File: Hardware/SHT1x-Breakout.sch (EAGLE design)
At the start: 9 parts, among them U1 SHT1XSMD

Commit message: Initial Revision Commit
Testing to make sure changes only happen to V_1.4 branch. Initial
layout of new revision.
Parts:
- removed R2: 10K, SparkFun:RESISTOR0603-RES
- removed U$1: LOGO-SFENEW, SparkFun:LOGO-SFENEW
- removed U$2, U$3: FIDUCIAL1X2, SparkFun:FIDUCIAL1X2
- added FID1, FID2: FIDUCIAL1X2, SparkFun-Aesthetics:FIDUCIAL1X2
- added FRAME1: (no value), SparkFun-Aesthetics:FRAME-LETTER
- added LOGO1: OSHW-LOGOS, SparkFun-Aesthetics:OSHW-LOGOS
- added LOGO4: SFE_LOGO_FLAME.1_INCH, SparkFun-Aesthetics:SFE_LOGO_FLAME.1_INCH
- added SJ1: JUMPER-PAD-2-NC_BY_TRACE, SparkFun-Passives:JUMPER-PAD-2-NC_BY_TRACE
- added STANDOFF1, STANDOFF2: STAND-OFF, SparkFun-Electromechanical:STAND-OFF
- C1: device SparkFun:CAP0603-CAP -> SparkFun-Capacitors:0.1UF-25V(+80/-20%)(0603)
- R1: device SparkFun:RESISTOR0603-RES -> SparkFun-Resistors:10KOHM-1/10W-1%(0603)0603
- U1: device SparkFun:SHT1XSMD -> SparkFun-Sensors:SHT1XSMD
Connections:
- removed net VDD: C1.2, JP1.1, R1.2, U1.VDD
- new net N$1: R1.1, SJ1.1
- new net VCC: C1.1, JP1.3, R1.2, U1.VDD
- net DATA: now also SJ1.2; no longer R1.1
- net GND: now also C1.2; no longer C1.1, R2.2
- net SCK: now also JP1.1; no longer JP1.3, R2.1
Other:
- note added: "Connector"
- note added: "However, it can live on an I2C bus with other I2C devices without interfering."
- note added: "Pull-up Resistor"
- note added: "Sht_15 Sensor"
- note added: "The SHT_15 communicates using a 2-wire Serial Protocol, NOT I2C."
- note removed: "01"
- note removed: "Not Populated"
- note removed: "SHT1x Breakout Board"
- moved on the sheet: C1, JP1, R1, U1

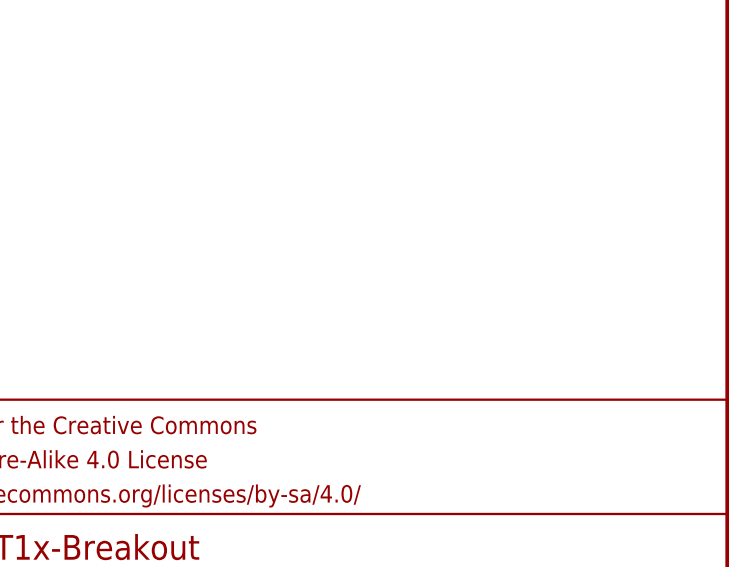
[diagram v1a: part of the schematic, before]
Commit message: Initial Layout finished
Initial Layout finished - ready for monday review
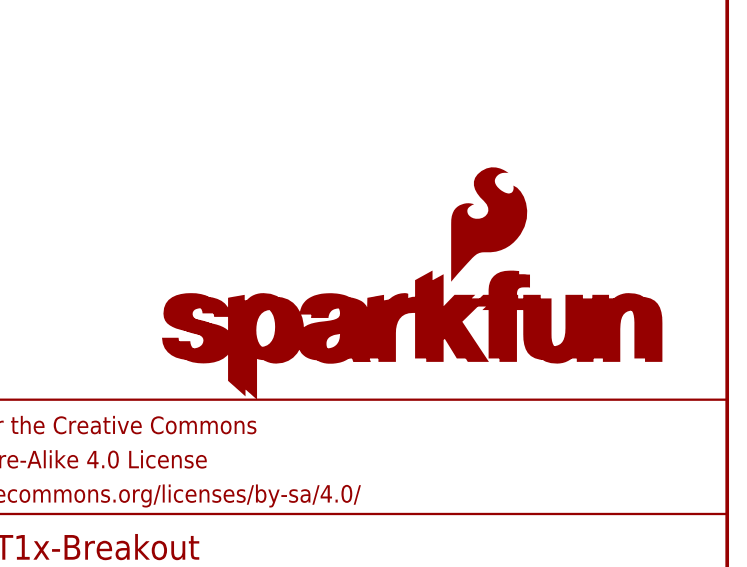
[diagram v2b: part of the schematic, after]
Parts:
- added LOGO2: SFE_LOGO_NAME.1_INCH, SparkFun-Aesthetics:SFE_LOGO_NAME.1_INCH
- added LOGO5: SFE_LOGO_NAME_FLAME.1_INCH, SparkFun-Aesthetics:SFE_LOGO_NAME_FLAME.1_INCH
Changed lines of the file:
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@@
 <part name="LOGO4" library="SparkFun-Aesthetics" deviceset="SFE_LOGO_FLAME" device=".1_INCH"/>
 <part name="P+2" library="SparkFun" deviceset="VCC" device=""/>
+<part name="LOGO2" library="SparkFun-Aesthetics" deviceset="SFE_LOGO_NAME" device=".1_INCH"/>
+<part name="LOGO5" library="SparkFun-Aesthetics" deviceset="SFE_LOGO_NAME_FLAME" device=".1_INCH"/>
 </parts>
 <sheets>
@@
 <instance part="LOGO4" gate="G$1" x="114.3" y="2.54"/>
 <instance part="P+2" gate="1" x="142.24" y="154.94"/>
+<instance part="LOGO2" gate="G$1" x="185.42" y="35.56"/>
+<instance part="LOGO5" gate="G$1" x="185.42" y="35.56"/>
 </instances>
 <busses>

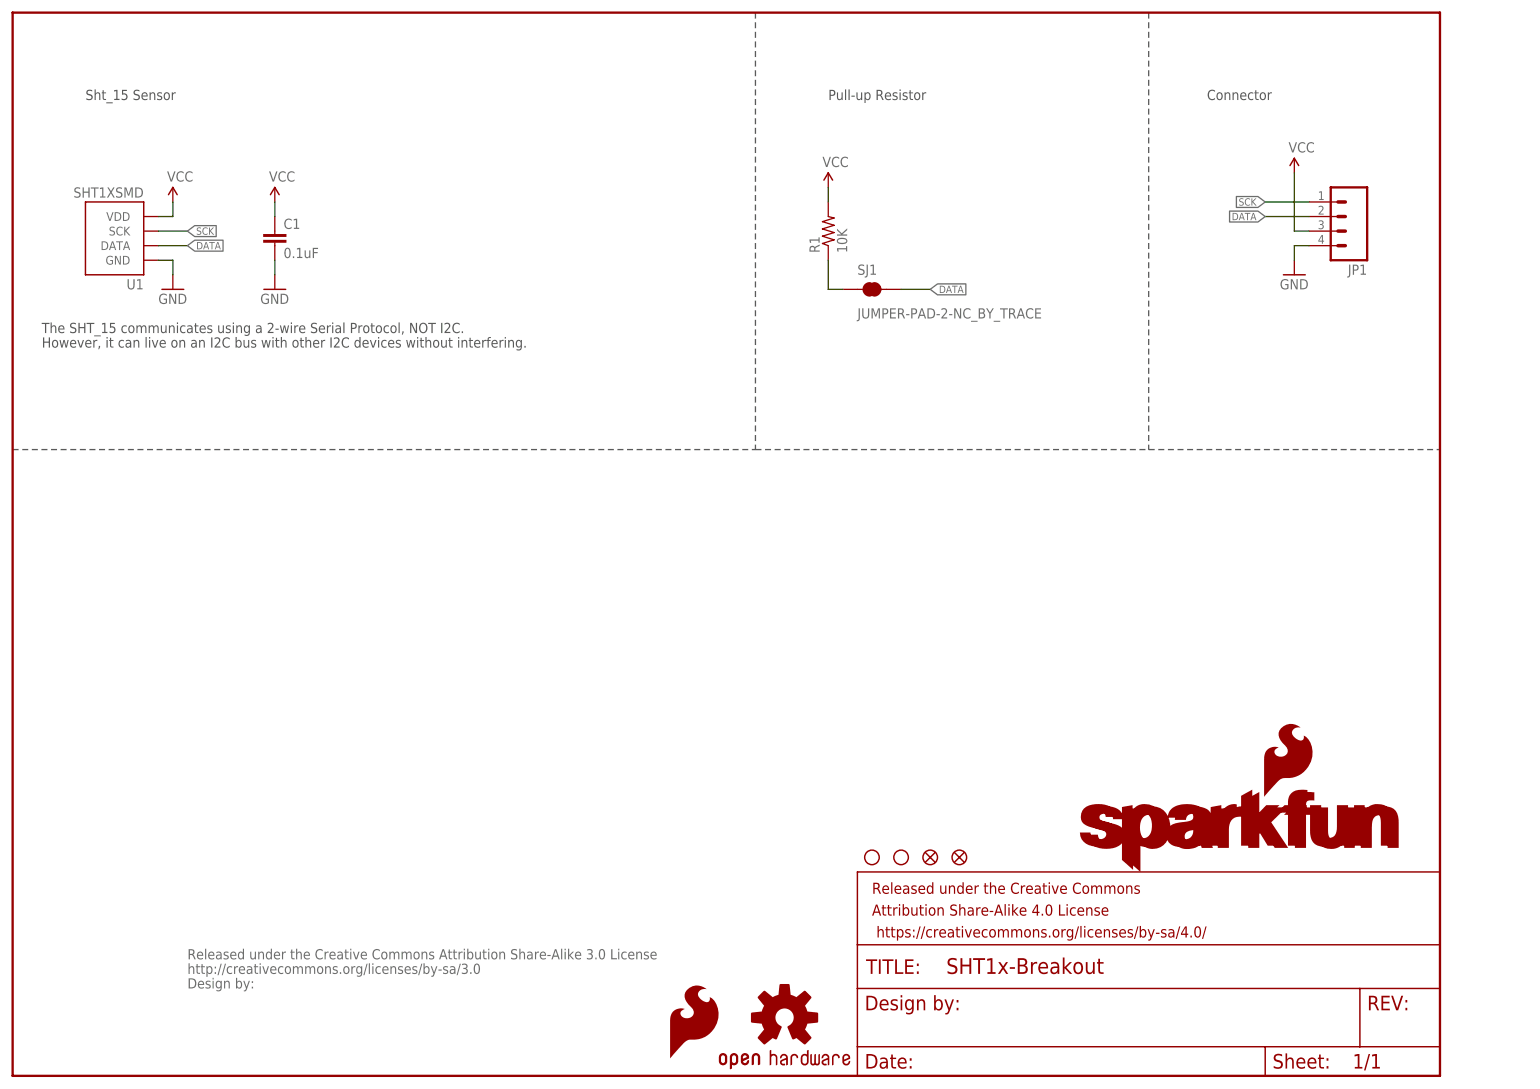
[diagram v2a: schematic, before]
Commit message: Monday Review Complete
Monday Review Changes implemented. Bottom silk on pins, names and
version numbers, + a few minor fixes.
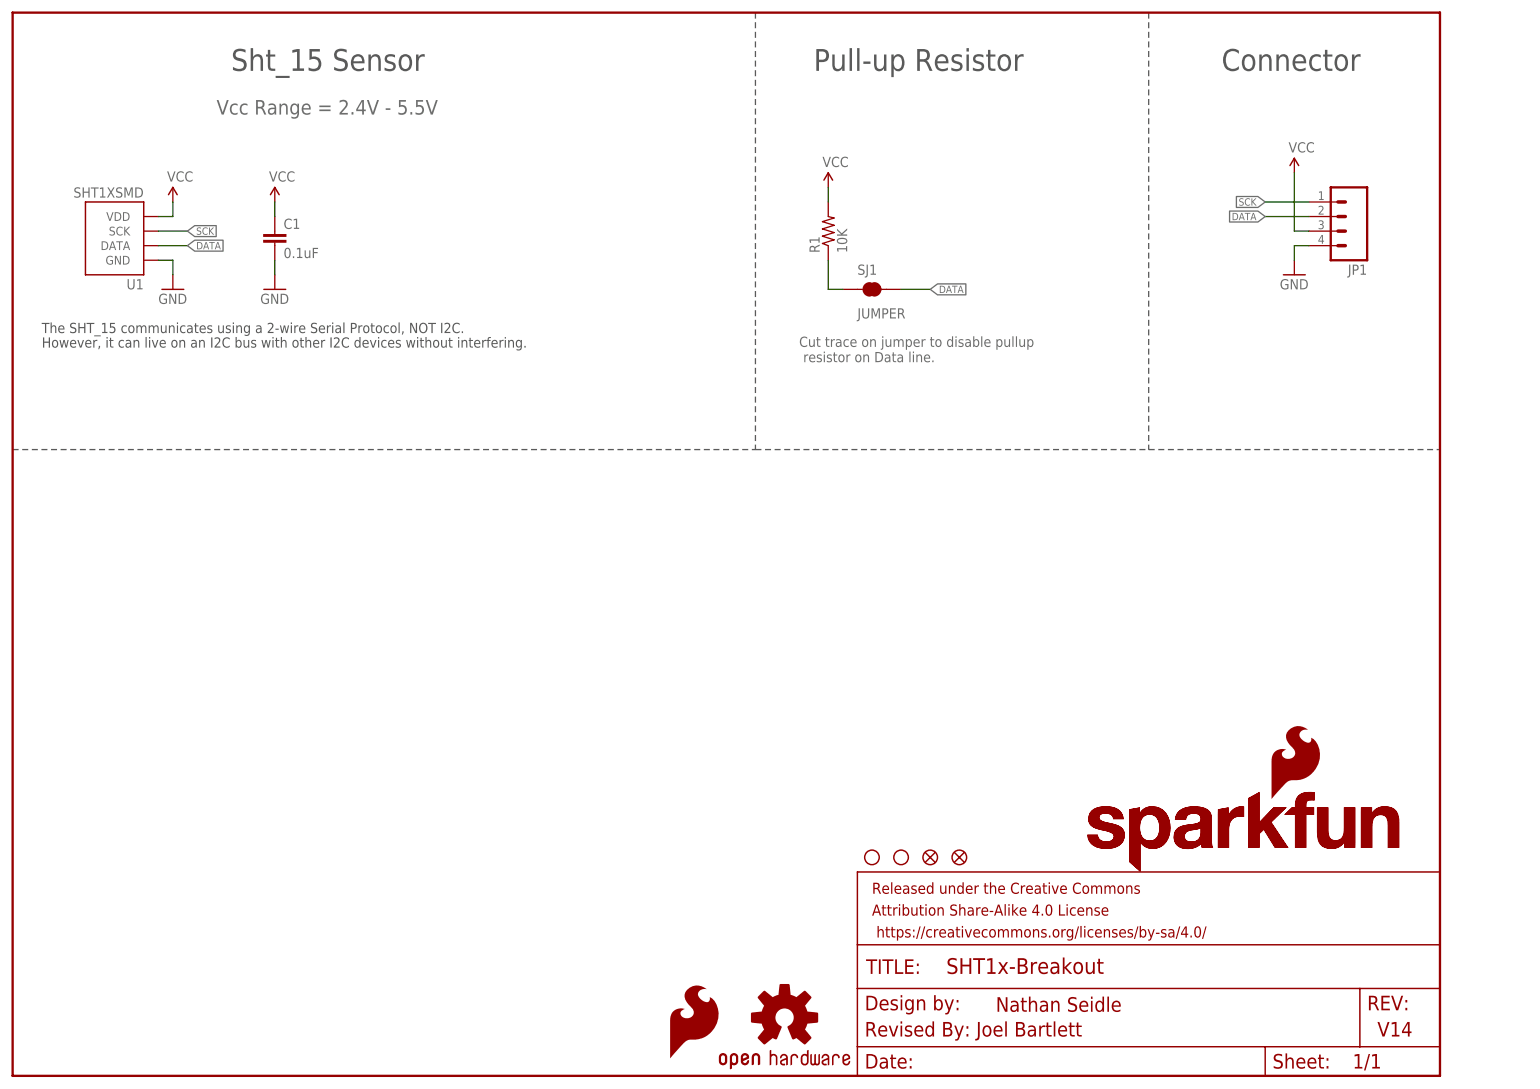
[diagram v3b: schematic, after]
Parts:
- removed U$4: CREATIVE_COMMONS, SparkFun:CREATIVE_COMMONS
- FRAME1: DESIGNER (none) -> Joel Bartlett; VERSION (none) -> v14
- SJ1: value JUMPER-PAD-2-NC_BY_TRACE -> JUMPER
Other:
- note added: "Cut trace on jumper to disable pullup resistor on Data line."
- note added: "Nathan Seidle"
- note added: "Revised By: Joel Bartlett"
- note added: "V14"
- note added: "Vcc Range = 2.4V - 5.5V"
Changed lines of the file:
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@@
 <setting verticaltext="up"/>
 </settings>
-<grid distance="0.1" unitdist="inch" unit="inch" style="lines" multiple="1" display="no" altdistance="0.01" altunitdist="inch" altunit="inch"/>
+<grid distance="0.1" unitdist="inch" unit="inch" style="lines" multiple="1" display="no" altdistance="0.001" altunitdist="inch" altunit="inch"/>
 <layers>
 <layer number="1" name="Top" color="4" fill="1" visible="no" active="no"/>
@@
 <part name="JP1" library="SparkFun" deviceset="M04" device="PTH"/>
 <part name="P+1" library="SparkFun" deviceset="VCC" device=""/>
-<part name="U$4" library="SparkFun" deviceset="CREATIVE_COMMONS" device=""/>
 <part name="U1" library="SparkFun-Sensors" deviceset="SHT1X" device="SMD"/>
 <part name="P+3" library="SparkFun" deviceset="VCC" device=""/>
@@
 <part name="GND2" library="SparkFun" deviceset="GND" device=""/>
 <part name="R1" library="SparkFun-Resistors" deviceset="10KOHM-1/10W-1%(0603)" device="0603" value="10K"/>
-<part name="SJ1" library="SparkFun-Passives" deviceset="JUMPER-PAD-2-NC_BY_TRACE" device=""/>
+<part name="SJ1" library="SparkFun-Passives" deviceset="JUMPER-PAD-2-NC_BY_TRACE" device="" value="JUMPER"/>
 <part name="STANDOFF1" library="SparkFun-Electromechanical" deviceset="STAND-OFF" device=""/>
 <part name="STANDOFF2" library="SparkFun-Electromechanical" deviceset="STAND-OFF" device=""/>
-<part name="FRAME1" library="SparkFun-Aesthetics" deviceset="FRAME-LETTER" device=""/>
+<part name="FRAME1" library="SparkFun-Aesthetics" deviceset="FRAME-LETTER" device="">
+<attribute name="DESIGNER" value="Joel Bartlett"/>
+<attribute name="VERSION" value="v14"/>
+</part>
 <part name="LOGO1" library="SparkFun-Aesthetics" deviceset="OSHW-LOGO" device="S"/>
 <part name="FID1" library="SparkFun-Aesthetics" deviceset="FIDUCIAL" device="1X2"/>
@@
 <sheet>
 <plain>
-<text x="12.7" y="170.18" size="1.778" layer="97">Sht_15 Sensor</text>
+<text x="38.1" y="175.26" size="3.81" layer="97">Sht_15 Sensor</text>
 <text x="5.08" y="129.54" size="1.778" layer="97">The SHT_15 communicates using a 2-wire Serial Protocol, NOT I2C.</text>
 <text x="5.08" y="127" size="1.778" layer="97">However, it can live on an I2C bus with other I2C devices without interfering.</text>
-<text x="208.28" y="170.18" size="1.778" layer="97">Connector</text>
-<text x="142.24" y="170.18" size="1.778" layer="97">Pull-up Resistor</text>
+<text x="210.82" y="175.26" size="3.81" layer="97">Connector</text>
+<text x="139.7" y="175.26" size="3.81" layer="97">Pull-up Resistor</text>
 <wire x1="0" y1="109.22" x2="129.54" y2="109.22" width="0.1524" layer="97" style="shortdash"/>
 <wire x1="129.54" y1="109.22" x2="198.12" y2="109.22" width="0.1524" layer="97" style="shortdash"/>
@@
 <wire x1="129.54" y1="185.42" x2="129.54" y2="109.22" width="0.1524" layer="97" style="shortdash"/>
 <wire x1="198.12" y1="185.42" x2="198.12" y2="109.22" width="0.1524" layer="97" style="shortdash"/>
+<text x="171.45" y="11.176" size="2.54" layer="94">Nathan Seidle</text>
+<text x="237.998" y="6.858" size="2.54" layer="94">V14</text>
+<text x="148.59" y="6.858" size="2.54" layer="94">Revised By: Joel Bartlett</text>
+<text x="35.56" y="167.64" size="2.54" layer="96">Vcc Range = 2.4V - 5.5V</text>
+<text x="137.16" y="124.46" size="1.778" layer="96">Cut trace on jumper to disable pullup
+ resistor on Data line.</text>
 </plain>
 <instances>
@@
 <instance part="JP1" gate="G$1" x="231.14" y="149.86" rot="R180"/>
 <instance part="P+1" gate="1" x="45.72" y="152.4"/>
-<instance part="U$4" gate="G$1" x="30.48" y="15.24"/>
 <instance part="U1" gate="G$1" x="17.78" y="147.32" rot="R180"/>
 <instance part="P+3" gate="1" x="27.94" y="152.4"/>
@@
 <instance part="STANDOFF2" gate="G$1" x="154.94" y="38.1"/>
 <instance part="FRAME1" gate="G$1" x="0" y="0"/>
-<instance part="FRAME1" gate="V" x="147.32" y="0"/>
+<instance part="FRAME1" gate="V" x="147.32" y="0" smashed="yes">
+<attribute name="LAST_DATE_TIME" x="160.02" y="1.27" size="2.54" layer="94" font="vector"/>
+<attribute name="SHEET" x="233.68" y="1.27" size="2.54" layer="94" font="vector"/>
+<attribute name="DRAWING_NAME" x="162.814" y="17.78" size="2.7432" layer="94" font="vector"/>
+</instance>
 <instance part="LOGO1" gate="G$1" x="134.62" y="10.16"/>
 <instance part="FID1" gate="G$1" x="160.02" y="38.1"/>
@@
 <instance part="P+2" gate="1" x="142.24" y="154.94"/>
 <instance part="LOGO2" gate="G$1" x="185.42" y="35.56"/>
-<instance part="LOGO5" gate="G$1" x="185.42" y="35.56"/>
+<instance part="LOGO5" gate="G$1" x="186.7154" y="35.179"/>
 </instances>
 <busses>
@@
 </schematic>
 </drawing>
+<compatibility>
+<note version="6.3" minversion="6.2.2" severity="warning">
+Since Version 6.2.2 text objects can contain more than one line,
+which will not be processed correctly with this version.
+</note>
+</compatibility>
 </eagle>

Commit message: Ready for final QC approval before protos
Addressed QC issues. Minor route changes. Added PROD_ID to SHT_15.
Altered silk name to match website name.
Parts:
- FRAME1: value (none) -> FRAME-LETTER; DESIGNER Joel Bartlett -> (none); VERSION v14 -> (none)
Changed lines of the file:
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@@
 <setting verticaltext="up"/>
 </settings>
-<grid distance="0.1" unitdist="inch" unit="inch" style="lines" multiple="1" display="no" altdistance="0.001" altunitdist="inch" altunit="inch"/>
+<grid distance="0.1" unitdist="inch" unit="inch" style="lines" multiple="1" display="no" altdistance="0.01" altunitdist="inch" altunit="inch"/>
 <layers>
 <layer number="1" name="Top" color="4" fill="1" visible="no" active="no"/>
@@
 <layer number="113" name="IDFDebug" color="7" fill="1" visible="yes" active="yes"/>
 <layer number="116" name="Patch_BOT" color="9" fill="4" visible="yes" active="yes"/>
+<layer number="118" name="Rect_Pads" color="7" fill="1" visible="yes" active="yes"/>
 <layer number="121" name="_tsilk" color="7" fill="1" visible="yes" active="yes"/>
 <layer number="122" name="_bsilk" color="7" fill="1" visible="yes" active="yes"/>
@@
 <part name="STANDOFF1" library="SparkFun-Electromechanical" deviceset="STAND-OFF" device=""/>
 <part name="STANDOFF2" library="SparkFun-Electromechanical" deviceset="STAND-OFF" device=""/>
-<part name="FRAME1" library="SparkFun-Aesthetics" deviceset="FRAME-LETTER" device="">
-<attribute name="DESIGNER" value="Joel Bartlett"/>
-<attribute name="VERSION" value="v14"/>
-</part>
+<part name="FRAME1" library="SparkFun-Aesthetics" deviceset="FRAME-LETTER" device=""/>
 <part name="LOGO1" library="SparkFun-Aesthetics" deviceset="OSHW-LOGO" device="S"/>
 <part name="FID1" library="SparkFun-Aesthetics" deviceset="FIDUCIAL" device="1X2"/>
